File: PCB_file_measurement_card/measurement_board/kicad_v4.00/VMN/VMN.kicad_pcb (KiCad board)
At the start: 2 copper layers, 47 parts, among them J1 A/B, J2 Screw_Terminal_VMN, J3 Alim DPH5005, J4 Raspberry_Pi_2_3, J5 Screw_Terminal_01x02, K1 AQY211EH, K2 AQY211EH, K3 AQY211EH, K4 AQY211EH, U1 INA128, U2 MCP23008-xP, U3 LM358, U4 INA282, U5 1085-Adress=0X49, U6 1085-Adress=0X48, U7 ISO1540

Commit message: Fixes some footprints and Adds first PCB rules and layout
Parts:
- J4: footprint Connector_PinHeader_2.54mm:PinHeader_2x20_P2.54mm_Vertical -> Connector_PinSocket_2.54mm:PinSocket_2x20_P2.54mm_Vertical; moved to B.Cu
- R6: footprint Resistor_THT:R_Axial_DIN0411_L9.9mm_D3.6mm_P15.24mm_Horizontal -> Resistor_THT:R_Axial_DIN0414_L11.9mm_D4.5mm_P20.32mm_Horizontal
- moved J5 184.8 mm to (63.5, 180.3)
- moved J1 179.9 mm to (251.5, 167.6), turned to 90 degrees
- moved R1 169.4 mm to (221.0, 154.9), turned to 180 degrees
- moved R2 164.9 mm to (221.0, 147.3), turned to 180 degrees
- moved R6 162.7 mm to (228.6, 114.3), turned to 180 degrees
- moved Alim_analog_Vmn1 153.4 mm to (27.9, 149.9), turned to 90 degrees
- moved U5 152.7 mm to (240.0, 133.3), turned to -90 degrees
- moved J3 152.6 mm to (226.1, 180.3)
- moved K3 150.3 mm to (231.1, 149.9)
- moved K2 149.5 mm to (231.1, 157.5)
- moved K1 145.7 mm to (231.1, 165.1)
- moved K4 139.4 mm to (231.1, 142.2)
- moved C12 138.4 mm to (215.9, 132.1), turned to 180 degrees
- moved J2 134.1 mm to (170.2, 195.6)
- moved D4 126.2 mm to (171.4, 137.2)
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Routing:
- net SCL1: track 0.00 -> 9.66 mm
- net SDA1: track 0.00 -> 9.58 mm
- net 5VD: track 0.00 -> 6.68 mm
- net GNDD: track 0.00 -> 6.57 mm

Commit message: Adds a first version of the PCB to be checked...
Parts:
- moved C5 146.5 mm to (55.9, 91.4)
- moved C4 146.5 mm to (61.0, 101.6)
- moved C6 146.5 mm to (68.6, 99.1)
- moved U1 146.5 mm to (47.0, 102.9)
- moved J2 143.8 mm to (48.3, 119.4)
- moved R4 138.4 mm to (60.8, 51.0), turned to 0 degrees
- moved U3 137.3 mm to (64.6, 57.3), turned to -90 degrees
- moved C3 136.0 mm to (66.0, 91.4)
- moved R3 129.6 mm to (61.0, 83.8), turned to 180 degrees
- moved D4 128.4 mm to (70.9, 57.3), turned to -90 degrees
- moved D2 125.2 mm to (62.0, 71.3), turned to 180 degrees
- moved D3 120.3 mm to (76.0, 65.0), turned to 90 degrees
- moved C14 119.1 mm to (152.4, 76.2)
- moved R7 93.2 mm to (142.2, 63.5), turned to 0 degrees
- moved U7 88.0 mm to (160.0, 73.7)
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- renumbered Alim_5V_Digital_rasp_iso1540_mcp1 to Alim_5V_Digital
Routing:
- net 5V: track 0.00 -> 203.3 mm
- net SDA2: track 0.00 -> 149.9 mm, vias 0 -> 1
- net SCL2: track 0.00 -> 144.2 mm, vias 0 -> 1
- net +12.5V: track 0.00 -> 136.4 mm
- net GNDPWR: track 0.00 -> 135.0 mm
- net -12V: track 0.00 -> 110.9 mm
- net 5VD: track 6.68 -> 116.7 mm
- net Net-(J3-Pad1): track 0.00 -> 85.6 mm, vias 0 -> 1
- net Net-(J3-Pad2): track 0.00 -> 84.9 mm
- net Net-(K1-Pad4): track 0.00 -> 79.1 mm, vias 0 -> 1
- net 12V: track 0.00 -> 65.8 mm
- net Net-(R1-Pad2): track 0.00 -> 65.0 mm
- net Net-(D1-Pad2): track 0.00 -> 62.2 mm
- net Net-(R2-Pad2): track 0.00 -> 54.7 mm
- net B: track 0.00 -> 47.1 mm
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- added copper zone on B.Cu, net GNDA
- added copper zone on F.Cu, net GNDA
- added copper zone on B.Cu, net GNDD
- added copper zone on F.Cu, net GNDD
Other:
- board outline added: 203.2 x 86.4 mm
- board text added: "+12V GND RX POWER"
- board text added: "+VDC GND TX POWER"
- board text added: "B / A"
- board text added: "M / N"
- board text added: "OhmPi measurement board v4.00 - OhmPi Team https://reversaal.gitlab.irstea.page/OhmPi"

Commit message: update pcb board
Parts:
- R10: footprint Resistor_THT:R_Axial_DIN0411_L9.9mm_D3.6mm_P15.24mm_Horizontal -> Resistor_THT:R_Axial_DIN0207_L6.3mm_D2.5mm_P7.62mm_Horizontal
- U3: value LM358 -> LM158
- moved C10 13.3 mm to (46.0, 58.0), turned to 0 degrees
- moved C9 3.92 mm to (66.0, 75.0)
- moved C8 2.62 mm to (53.0, 57.5)
- moved C7 2.30 mm to (65.9, 69.0)
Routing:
- net 5VD: track 116.7 -> 125.2 mm
- net -12V: track 110.9 -> 113.7 mm
- net SDA1: track 56.2 -> 57.5 mm
- net SCL2: track 144.2 -> 145.4 mm

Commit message: update pcb board
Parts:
- added REF**: Hole_3.2mm_M3, MountingHole:MountingHole_3.2mm_M3_ISO7380, F.Cu at (45.0, 49.0)
- added REF**: Hole_3.2mm_M3, MountingHole:MountingHole_3.2mm_M3_ISO7380, F.Cu at (45.0, 124.0)
- R3, R5: footprint Resistor_THT:R_Axial_DIN0411_L9.9mm_D3.6mm_P15.24mm_Horizontal -> Resistor_THT:R_Axial_DIN0207_L6.3mm_D2.5mm_P7.62mm_Horizontal
- moved C3 11.0 mm to (55.0, 91.4), turned to 90 degrees
- moved R5 7.47 mm to (53.2, 78.7)
- moved J2 7.27 mm to (55.5, 118.3)
- moved C5 6.96 mm to (49.0, 92.5), turned to 90 degrees
- moved C6 5.58 mm to (63.0, 99.0)
- moved C4 3.27 mm to (58.0, 103.0)
- moved C14 1.60 mm to (154.0, 76.2)
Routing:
- net Net-(J3-Pad1): track 85.6 -> 101.8 mm
- net Net-(R3-Pad2): track 26.2 -> 22.1 mm
- net Net-(R3-Pad1): track 43.1 -> 45.9 mm
- net Net-(J2-Pad2): track 17.0 -> 19.7 mm
- net +12.5V: track 136.4 -> 139.0 mm
- net -12V: track 113.7 -> 115.9 mm
- net Net-(J2-Pad1): track 17.1 -> 19.0 mm
- net 12V: track 65.8 -> 67.5 mm
- net 5VD: track 125.2 -> 124.3 mm

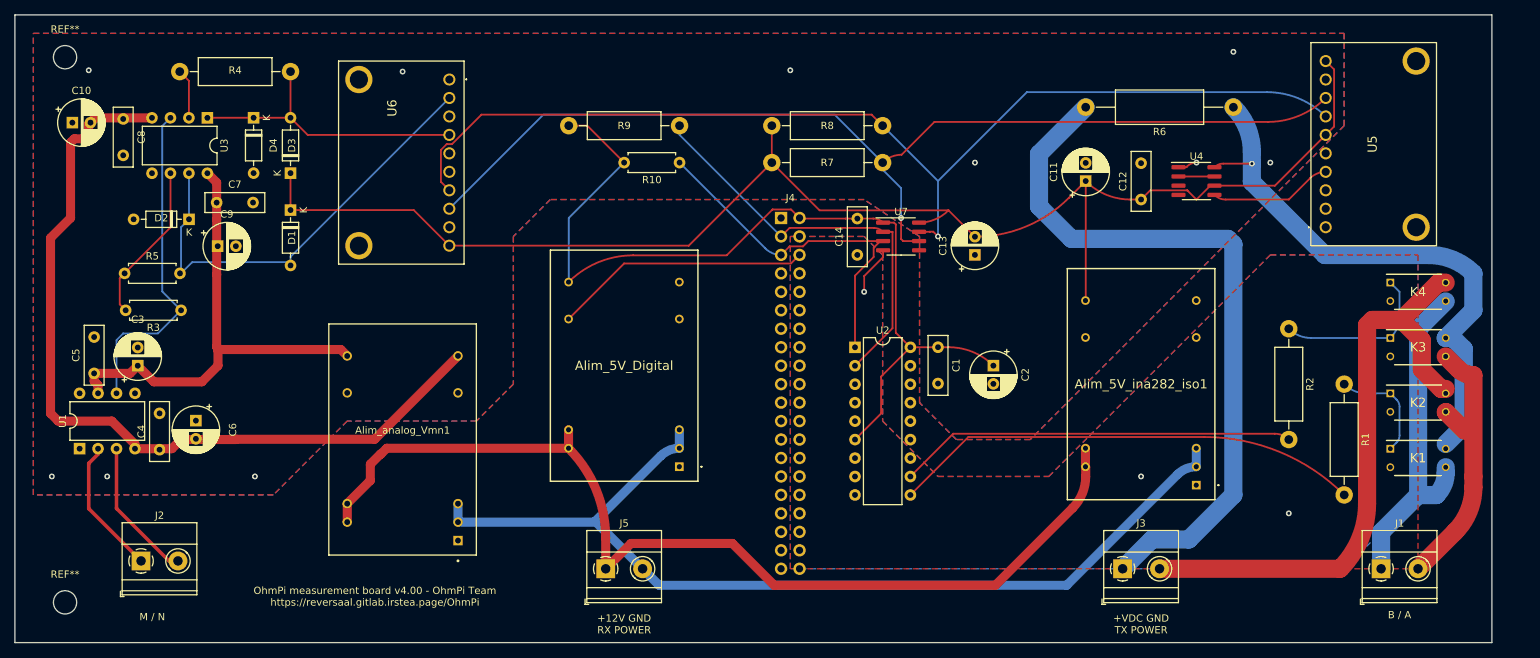
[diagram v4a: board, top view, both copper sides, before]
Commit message: Improvements of measurement card v4.00 - change resistors to smaller footprint, adds MUX connector, adds mounting holes
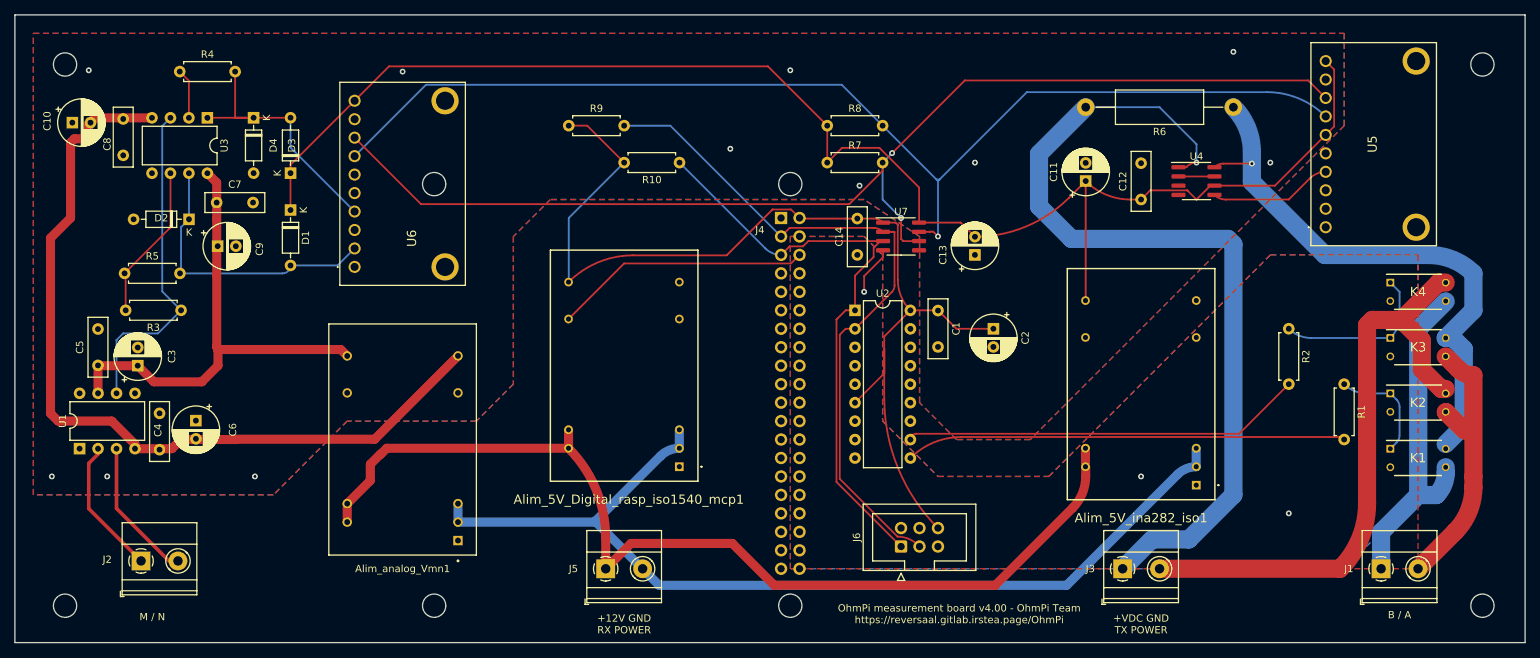
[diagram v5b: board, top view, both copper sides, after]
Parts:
- added J6: Conn_02x03_Top_Bottom, Connector_IDC:IDC-Header_2x03_P2.54mm_Vertical, F.Cu at (160.0, 116.3)
- added REF**: Hole_3.2mm_M3, MountingHole:MountingHole_3.2mm_M3_ISO7380, F.Cu at (95.8, 124.5)
- added REF**: Hole_3.2mm_M3, MountingHole:MountingHole_3.2mm_M3_ISO7380, F.Cu at (144.8, 124.5)
- added REF**: Hole_3.2mm_M3, MountingHole:MountingHole_3.2mm_M3_ISO7380, F.Cu at (95.8, 66.5)
- added REF**: Hole_3.2mm_M3, MountingHole:MountingHole_3.2mm_M3_ISO7380, F.Cu at (240.0, 124.5)
- added REF**: Hole_3.2mm_M3, MountingHole:MountingHole_3.2mm_M3_ISO7380, F.Cu at (45.0, 50.0)
- added REF**: Hole_3.2mm_M3, MountingHole:MountingHole_3.2mm_M3_ISO7380, F.Cu at (144.8, 66.5)
- R1, R2, R4, R7, R8, R9: footprint Resistor_THT:R_Axial_DIN0411_L9.9mm_D3.6mm_P15.24mm_Horizontal -> Resistor_THT:R_Axial_DIN0207_L6.3mm_D2.5mm_P7.62mm_Horizontal
- U3: value LM158 -> LM358
- moved REF** 195.0 mm to (240.0, 50.0)
- moved U6 28.9 mm to (84.8, 77.9), turned to -90 degrees
- moved R7 7.62 mm to (149.9, 63.5)
- moved R8 7.62 mm to (149.9, 58.4)
- moved C2 5.08 mm to (172.7, 86.4)
- moved U2 5.08 mm to (153.7, 83.8)
- moved C1 5.04 mm to (165.1, 83.9)
- moved C5 1.22 mm to (49.5, 91.4)
- moved REF** 0.46 mm to (45.0, 124.5)
- renumbered Alim_5V_Digital to Alim_5V_Digital_rasp_iso1540_mcp1
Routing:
- net SDA1: track 57.5 -> 96.6 mm
- net SCL1: track 50.3 -> 83.3 mm
- net Net-(D1-Pad2): track 62.2 -> 39.8 mm
- net 5VD: track 124.3 -> 146.0 mm
- net Net-(J3-Pad1): track 101.8 -> 121.7 mm
- net SCL2: track 145.8 -> 160.3 mm, vias 1 -> 2
- net SDA2: track 150.0 -> 159.7 mm
- net Net-(R1-Pad2): track 65.0 -> 60.6 mm
- net Net-(D3-Pad2): track 40.6 -> 36.9 mm
- net 5V: track 203.3 -> 206.7 mm
- net Net-(R2-Pad2): track 54.7 -> 55.3 mm
- net GNDA: vias 9 -> 11
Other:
- board size 203.2 x 86.4 mm -> 207.8 x 86.4 mm

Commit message: update pcb
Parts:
- moved C13 7.52 mm to (168.0, 69.0), turned to -90 degrees
- moved C11 4.68 mm to (190.0, 67.0)
- moved C12 2.24 mm to (195.0, 67.5)
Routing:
- net SDA2: track 159.7 -> 177.1 mm
- net 5V: track 206.7 -> 203.4 mm
- net SCL2: track 160.3 -> 163.1 mm
- net 5VD: track 146.0 -> 146.6 mm

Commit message: bord V5
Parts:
- U3: value LM358 -> LM158
- moved C11 13.4 mm to (202.0, 73.0), turned to 0 degrees
- moved C12 4.30 mm to (197.5, 71.0), turned to 180 degrees
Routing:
- net 5V: track 203.4 -> 213.1 mm
- net SCL2: track 163.1 -> 169.3 mm
- net SCL1: track 83.3 -> 88.3 mm
- net 5VD: track 146.6 -> 151.6 mm
- net SDA1: track 96.6 -> 101.3 mm
- net A: track 37.7 -> 40.8 mm
- net +12.5V: track 139.0 -> 140.1 mm
- net Net-(K1-Pad4): track 79.2 -> 80.0 mm
- net Net-(J3-Pad2): track 84.9 -> 85.5 mm
